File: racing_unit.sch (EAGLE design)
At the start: 45 parts, among them IC1 7805, IC2 7805, IC3 7805, IC4 7805, Q1 MJE2955, Q2 MJE2955, Q3 MJE2955, Q4 MJE2955

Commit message: updated schematic
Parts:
- removed ARD-COIL1, ARD-COIL2, ARD-COIL4, ARD_COIL3: (no value), con-ptr500:AK500/2
- removed C2, C3: 470uF/25V, rcl:CPOL-EUE3.5-8
- added ARDUINI_1-12, ARDUINO_13-24: (no value), pinhead:PINHD-1X12
- added HC-06: (no value), pinhead:PINHD-1X4
- added LED1: (no value), led:LED3MM
- added MPU6050: (no value), pinhead:PINHD-1X8
- added QS_SENSOR: (no value), con-ptr500:AK500/2
- added R13: 150R, resistor:R-EU_0204/5
- added R14: 330R, resistor:R-EU_0204/5
- R6: value 1k -> 2k2
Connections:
- new net N$13: LED1.A, R13.1
- new net N$27: ARDUINI_1-12.6, MPU6050.3, R8.1
- new net N$28: ARDUINI_1-12.2, R5.2
- new net N$30: ARDUINO_13-24.1, C1.+, C4.+, D1.C, D2.C, D3.C, D4.C, R13.2, SUPPLY-1.KL
- new net N$32: HC-06.3, R5.1, R6.1
- net N$16: now also ARDUINO_13-24.8, QS_SENSOR-1.KL, R14.1; no longer ARD-COIL2-1.KL, R6.1
- net N$18: now also ARDUINI_1-12.5, MPU6050.4, R7.1; no longer C1.+, C2.+, C3.+, C4.+, D1.C, D2.C, D3.C, D4.C, SUPPLY-1.KL
- net N$19: now also ARDUINI_1-12.9; no longer R7.2
- net N$20: now also ARDUINI_1-12.10, MPU6050.8; no longer ARD_COIL3-1.KL, R7.1
- net N$22: now also ARDUINI_1-12.1, HC-06.4; no longer ARD-COIL4-1.KL, R8.1
- net N$23: now also ARDUINO_13-24.12; no longer ARD-COIL1-2.KL
- net N$24: now also ARDUINO_13-24.11; no longer ARD-COIL2-2.KL
- net N$25: now also ARDUINO_13-24.10; no longer ARD_COIL3-2.KL
- net N$26: now also ARDUINO_13-24.9; no longer ARD-COIL4-2.KL
- net N$5: now also ARDUINO_13-24.4, HC-06.1, MPU6050.1, MPU6050.7, QS_SENSOR-2.KL, R7.2, R8.2; no longer ARD-COIL1-1.KL, R5.1
- net N$6: now also ARDUINI_1-12.12; no longer R5.2
- net N$7: now also ARDUINI_1-12.11; no longer R6.2
- net N$8: now also ARDUINI_1-12.8; no longer R8.2
- net PE: now also ARDUINI_1-12.3, ARDUINI_1-12.4, ARDUINO_13-24.2, HC-06.2, LED1.C, MPU6050.2, R14.2, R6.2; no longer C2.-, C3.-
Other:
- moved on the sheet: C1, C4, D1, D2, D3, D4, R10, R11, R12, R5, R6, R7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

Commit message: added pcb design
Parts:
- removed C4: 470uF/25V, rcl:CPOL-EUE3.5-8
- removed LED1: (no value), led:LED3MM
- added C2: 4700uF/25V, rcl:CPOL-EUE7.5-16
- added J1, J2: J10MM, jumper:J10MM
- added J3, J4, J7, J8, J9: J5MM, jumper:J5MM
- added J5, J6: J7MM, jumper:J7MM
- added LED: (no value), pinhead:PINHD-1X2
- C1: value 470uF/25V -> 4700uF/25V; device rcl:CPOL-EUE3.5-8 -> rcl:CPOL-EUE7.5-16
- D1, D2, D3, D4: value 1N4007 -> 1N4937
- IC1, IC2, IC3, IC4: value 7805 -> 78L05Z; device v-reg:78XXS -> linear:78L05Z
- Q1, Q2, Q3, Q4: value MJE2955 -> BDX54C
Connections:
- removed net PE: ARDUINI_1-12.3, ARDUINI_1-12.4, ARDUINO_13-24.2, C1.-, C10.2, C11.2, C12.2, C4.-, C5.2, C6.2, C7.2, C8.2, C9.2, HC-06.2, IC1.GND, IC2.GND, IC3.GND, IC4.GND, LED1.C, MPU6050.2, R1.1, R14.2, R2.1, R3.1, R4.1, R6.2, SUPPLY-2.KL
- new net GND: ARDUINI_1-12.3, ARDUINI_1-12.4, ARDUINO_13-24.2, C1.-, C10.2, C11.2, C12.2, C2.-, C5.2, C6.2, C7.2, C8.2, C9.2, HC-06.2, IC1.GND, IC2.GND, IC3.GND, IC4.GND, LED.1, MPU6050.2, R1.1, R14.2, R2.1, R3.1, R4.1, R6.2, SUPPLY-2.KL
- new net N$29: ARDUINI_1-12.12, J3.1, R1.2
- new net N$31: ARDUINI_1-12.11, J4.2, R2.2
- new net N$33: ARDUINI_1-12.9, J5.2, R3.2
- new net N$34: ARDUINI_1-12.8, J6.2, R4.2
- new net N$35: J4.1, J7.1
- new net N$37: J8.2, Q3.B
- new net N$38: J5.1, J8.1
- new net N$40: J9.2, Q4.B
- new net N$41: J6.1, J9.1
- net N$1: now also IC1.VI; no longer IC1.IN
- net N$13: now also LED.2, R13.2; no longer LED1.A, R13.1
- net N$14: now also IC1.VO; no longer IC1.OUT
- net N$15: now also IC2.VO; no longer IC2.OUT
- net N$17: now also IC4.VO; no longer IC4.OUT
- net N$19: now also ARDUINO_13-24.1, C1.+, C2.+, D3.C, D4.C, J2.2, SUPPLY-1.KL; no longer ARDUINI_1-12.9, Q3.B, R3.2
- net N$2: now also IC2.VI; no longer IC2.IN
- net N$21: now also IC3.VO; no longer IC3.OUT
- net N$22: now also R5.2; no longer HC-06.4
- net N$28: now also J3.2, Q1.B; no longer ARDUINI_1-12.2, R5.2
- net N$3: now also IC3.VI; no longer IC3.IN
- net N$30: now also J7.2, Q2.B; no longer ARDUINO_13-24.1, C1.+, C4.+, D1.C, D2.C, D3.C, D4.C, R13.2, SUPPLY-1.KL
- net N$32: now also HC-06.4; no longer HC-06.3
- net N$4: now also IC4.VI; no longer IC4.IN
- net N$6: now also ARDUINI_1-12.2, HC-06.3; no longer ARDUINI_1-12.12, Q1.B, R1.2
- net N$7: now also D1.C, J1.1, R13.1; no longer ARDUINI_1-12.11, Q2.B, R2.2
- net N$8: now also D2.C, J1.2, J2.1; no longer ARDUINI_1-12.8, Q4.B, R4.2
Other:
- moved on the sheet: D4, Q2, Q3, Q4, R10, R11, R12, R13, R5, R6, R9, SUPPLY-1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

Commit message: fixed pcb
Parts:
- removed J6: J7MM, jumper:J7MM
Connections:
- removed net N$31 (its old number): ARDUINI_1-12.11, J4.2, R2.2
- removed net N$34: ARDUINI_1-12.8, J6.2, R4.2
- new net N$18: ARDUINO_13-24.4, J5.2, QS_SENSOR-2.KL, R8.2
- net N$20: now also J3.1; no longer MPU6050.8
- net N$27: now also J4.1; no longer MPU6050.3
- net N$28: now also ARDUINI_1-12.12, R1.2; no longer J3.2
- net N$29: now also J3.2, MPU6050.8; no longer ARDUINI_1-12.12, J3.1, R1.2
- net N$33: now also J4.2, MPU6050.3; no longer ARDUINI_1-12.9, J5.2, R3.2
- net N$35: now also ARDUINI_1-12.11, R2.2; no longer J4.1
- net N$38: now also ARDUINI_1-12.9, R3.2; no longer J5.1
- net N$41: now also ARDUINI_1-12.8, R4.2; no longer J6.1
- net N$5: now also J5.1; no longer ARDUINO_13-24.4, QS_SENSOR-2.KL, R8.2
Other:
- moved on the sheet: J3, J4, J5, R7, R8

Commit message: updated pcb and schematic
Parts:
- J3: value J5MM -> J10MM; device jumper:J5MM -> jumper:J10MM
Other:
- moved on the sheet: C1, C2, SUPPLY-2
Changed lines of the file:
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@@
 <?xml version="1.0" encoding="utf-8"?>
 <!DOCTYPE eagle SYSTEM "eagle.dtd">
-<eagle version="7.6.0">
+<eagle version="7.2.0">
 <drawing>
 <settings>
@@
 <layers>
 <layer number="1" name="Top" color="4" fill="11" visible="no" active="no"/>
+<layer number="2" name="Route2" color="1" fill="3" visible="no" active="no"/>
+<layer number="3" name="Route3" color="4" fill="3" visible="no" active="no"/>
+<layer number="4" name="Route4" color="1" fill="4" visible="no" active="no"/>
+<layer number="5" name="Route5" color="4" fill="4" visible="no" active="no"/>
+<layer number="6" name="Route6" color="1" fill="8" visible="no" active="no"/>
+<layer number="7" name="Route7" color="4" fill="8" visible="no" active="no"/>
+<layer number="8" name="Route8" color="1" fill="2" visible="no" active="no"/>
+<layer number="9" name="Route9" color="4" fill="2" visible="no" active="no"/>
+<layer number="10" name="Route10" color="1" fill="7" visible="no" active="no"/>
+<layer number="11" name="Route11" color="4" fill="7" visible="no" active="no"/>
+<layer number="12" name="Route12" color="1" fill="5" visible="no" active="no"/>
+<layer number="13" name="Route13" color="4" fill="5" visible="no" active="no"/>
+<layer number="14" name="Route14" color="1" fill="6" visible="no" active="no"/>
+<layer number="15" name="Route15" color="4" fill="6" visible="no" active="no"/>
 <layer number="16" name="Bottom" color="1" fill="1" visible="no" active="no"/>
 <layer number="17" name="Pads" color="2" fill="1" visible="no" active="no"/>
@@
 <part name="D3" library="diode" deviceset="1N4004" device="" value="1N4937"/>
 <part name="D4" library="diode" deviceset="1N4004" device="" value="1N4937"/>
-<part name="GND11" library="supply2" deviceset="PE" device="" value="GND"/>
 <part name="SUPPLY" library="con-ptr500" deviceset="AK500/2" device=""/>
 <part name="GND12" library="supply2" deviceset="PE" device="" value="GND"/>
@@
 <part name="GND15" library="supply2" deviceset="PE" device="" value="GND"/>
 <part name="C1" library="rcl" deviceset="CPOL-EU" device="E7.5-16" value="4700uF/25V"/>
-<part name="C2" library="rcl" deviceset="CPOL-EU" device="E7.5-16" value="4700uF/25V"/>
 <part name="IC1" library="linear" deviceset="78*" device="Z" technology="L05"/>
 <part name="IC2" library="linear" deviceset="78*" device="Z" technology="L05"/>
@@
 <part name="J8" library="jumper" deviceset="J" device="5MM"/>
 <part name="J9" library="jumper" deviceset="J" device="5MM"/>
-<part name="J3" library="jumper" deviceset="J" device="5MM"/>
 <part name="J4" library="jumper" deviceset="J" device="5MM"/>
 <part name="J5" library="jumper" deviceset="J" device="7MM"/>
+<part name="J3" library="jumper" deviceset="J" device="10MM"/>
+<part name="C2" library="rcl" deviceset="CPOL-EU" device="E7.5-16" value="4700uF/25V"/>
 </parts>
 <sheets>
@@
 <instance part="D3" gate="1" x="129.54" y="22.86" rot="R270"/>
 <instance part="D4" gate="1" x="180.34" y="22.86" rot="R270"/>
-<instance part="GND11" gate="PE" x="180.34" y="-15.24"/>
 <instance part="SUPPLY" gate="-1" x="195.58" y="-25.4" rot="R90"/>
-<instance part="SUPPLY" gate="-2" x="203.2" y="-25.4" rot="R90"/>
-<instance part="GND12" gate="PE" x="213.36" y="-2.54"/>
+<instance part="SUPPLY" gate="-2" x="200.66" y="-25.4" rot="R90"/>
+<instance part="GND12" gate="PE" x="205.74" y="-2.54"/>
 <instance part="COIL1" gate="-1" x="15.24" y="111.76" rot="R270"/>
 <instance part="COIL1" gate="-2" x="20.32" y="111.76" rot="R270"/>
@@
 <instance part="GND9" gate="PE" x="22.86" y="-35.56"/>
 <instance part="R14" gate="G$1" x="137.16" y="-30.48" rot="R90"/>
-<instance part="GND10" gate="PE" x="162.56" y="-15.24"/>
+<instance part="GND10" gate="PE" x="180.34" y="-20.32"/>
 <instance part="GND13" gate="PE" x="40.64" y="-33.02"/>
 <instance part="GND14" gate="PE" x="152.4" y="-30.48"/>
 <instance part="GND15" gate="PE" x="137.16" y="-50.8"/>
-<instance part="C1" gate="G$1" x="162.56" y="-2.54"/>
-<instance part="C2" gate="G$1" x="180.34" y="-2.54"/>
+<instance part="C1" gate="G$1" x="180.34" y="-2.54"/>
 <instance part="IC1" gate="A1" x="38.1" y="99.06"/>
 <instance part="IC2" gate="A1" x="86.36" y="99.06"/>
@@
 <instance part="J8" gate="1" x="91.44" y="60.96"/>
 <instance part="J9" gate="1" x="139.7" y="60.96"/>
-<instance part="J3" gate="1" x="73.66" y="-68.58"/>
 <instance part="J4" gate="1" x="129.54" y="-55.88"/>
 <instance part="J5" gate="1" x="121.92" y="-25.4" rot="R90"/>
+<instance part="J3" gate="1" x="73.66" y="-68.58"/>
+<instance part="C2" gate="G$1" x="162.56" y="-2.54"/>
 </instances>
 <busses>
@@
 </segment>
 <segment>
-<pinref part="GND11" gate="PE" pin="PE"/>
-<wire x1="180.34" y1="-7.62" x2="180.34" y2="-12.7" width="0.1524" layer="91"/>
-<pinref part="C2" gate="G$1" pin="-"/>
-</segment>
-<segment>
 <pinref part="GND12" gate="PE" pin="PE"/>
-<wire x1="213.36" y1="0" x2="213.36" y2="5.08" width="0.1524" layer="91"/>
+<wire x1="205.74" y1="0" x2="205.74" y2="5.08" width="0.1524" layer="91"/>
 <pinref part="SUPPLY" gate="-2" pin="KL"/>
-<wire x1="213.36" y1="5.08" x2="203.2" y2="5.08" width="0.1524" layer="91"/>
-<wire x1="203.2" y1="5.08" x2="203.2" y2="-20.32" width="0.1524" layer="91"/>
+<wire x1="205.74" y1="5.08" x2="200.66" y2="5.08" width="0.1524" layer="91"/>
+<wire x1="200.66" y1="5.08" x2="200.66" y2="-20.32" width="0.1524" layer="91"/>
 </segment>
 <segment>
@@
 <segment>
 <pinref part="GND10" gate="PE" pin="PE"/>
+<wire x1="180.34" y1="-7.62" x2="180.34" y2="-12.7" width="0.1524" layer="91"/>
+<pinref part="C1" gate="G$1" pin="-"/>
+<pinref part="C2" gate="G$1" pin="-"/>
+<wire x1="180.34" y1="-12.7" x2="180.34" y2="-17.78" width="0.1524" layer="91"/>
 <wire x1="162.56" y1="-7.62" x2="162.56" y2="-12.7" width="0.1524" layer="91"/>
-<pinref part="C1" gate="G$1" pin="-"/>
+<wire x1="162.56" y1="-12.7" x2="180.34" y2="-12.7" width="0.1524" layer="91"/>
+<junction x="180.34" y="-12.7"/>
 </segment>
 <segment>
@@
 <pinref part="ARDUINI_1-12" gate="G$1" pin="10"/>
 <wire x1="48.26" y1="-43.18" x2="55.88" y2="-43.18" width="0.1524" layer="91"/>
+<wire x1="48.26" y1="-68.58" x2="68.58" y2="-68.58" width="0.1524" layer="91"/>
 <pinref part="J3" gate="1" pin="1"/>
-<wire x1="48.26" y1="-68.58" x2="68.58" y2="-68.58" width="0.1524" layer="91"/>
 </segment>
 </net>
@@
 <pinref part="D4" gate="1" pin="C"/>
 <wire x1="129.54" y1="5.08" x2="162.56" y2="5.08" width="0.1524" layer="91"/>
+<pinref part="D3" gate="1" pin="C"/>
 <wire x1="162.56" y1="5.08" x2="180.34" y2="5.08" width="0.1524" layer="91"/>
-<pinref part="D3" gate="1" pin="C"/>
 <wire x1="180.34" y1="5.08" x2="180.34" y2="20.32" width="0.1524" layer="91"/>
 <wire x1="129.54" y1="20.32" x2="129.54" y2="5.08" width="0.1524" layer="91"/>
@@
 <junction x="180.34" y="5.08"/>
 <junction x="180.34" y="5.08"/>
-<wire x1="162.56" y1="5.08" x2="162.56" y2="0" width="0.1524" layer="91"/>
-<junction x="162.56" y="5.08"/>
+<wire x1="180.34" y1="5.08" x2="180.34" y2="0" width="0.1524" layer="91"/>
+<junction x="180.34" y="5.08"/>
 <pinref part="C1" gate="G$1" pin="+"/>
-<pinref part="C2" gate="G$1" pin="+"/>
-<wire x1="180.34" y1="0" x2="180.34" y2="5.08" width="0.1524" layer="91"/>
 <junction x="180.34" y="5.08"/>
 <pinref part="J2" gate="1" pin="2"/>
@@
 <wire x1="96.52" y1="-15.24" x2="129.54" y2="-15.24" width="0.1524" layer="91"/>
 <wire x1="129.54" y1="-15.24" x2="129.54" y2="5.08" width="0.1524" layer="91"/>
+<wire x1="162.56" y1="0" x2="162.56" y2="5.08" width="0.1524" layer="91"/>
+<junction x="162.56" y="5.08"/>
+<pinref part="C2" gate="G$1" pin="+"/>
 </segment>
 </net>
@@
 <net name="N$29" class="0">
 <segment>
-<pinref part="J3" gate="1" pin="2"/>
 <pinref part="MPU6050" gate="A" pin="8"/>
 <wire x1="78.74" y1="-68.58" x2="152.4" y2="-68.58" width="0.1524" layer="91"/>
-</segment>
-</net>
+<pinref part="J3" gate="1" pin="2"/>
+</segment>
+</net>

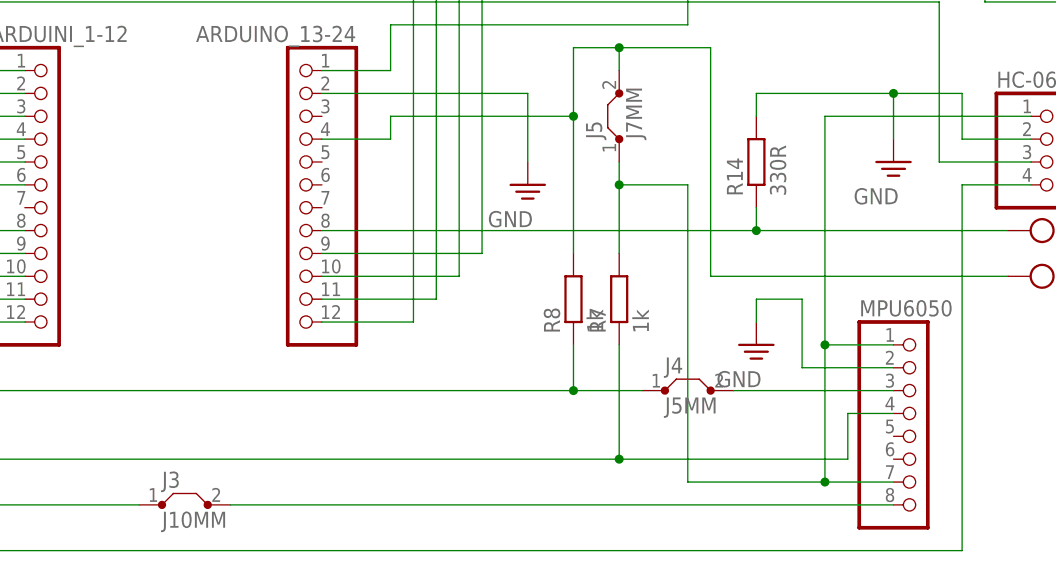
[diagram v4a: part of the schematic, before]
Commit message: updated pcb and improved spark killing procedure
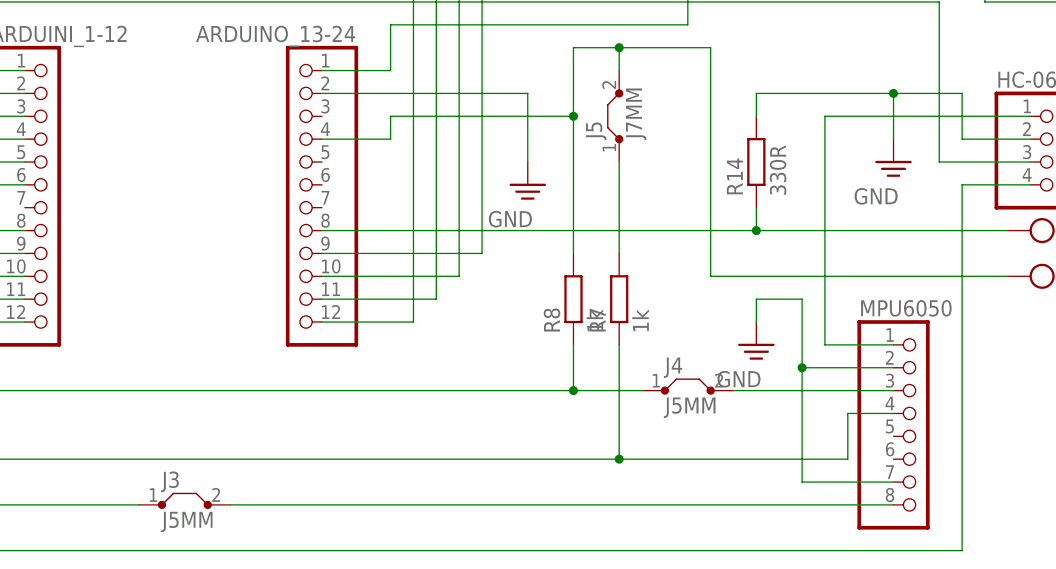
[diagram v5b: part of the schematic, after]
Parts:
- J3: value J10MM -> J5MM; device jumper:J10MM -> jumper:J5MM
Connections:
- removed net N$5: HC-06.1, J5.1, MPU6050.1, MPU6050.7, R7.2
- new net N$34: HC-06.1, MPU6050.1
- new net N$36: J5.1, R7.2
- net GND: now also MPU6050.7
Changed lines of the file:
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@@
 <part name="J4" library="jumper" deviceset="J" device="5MM"/>
 <part name="J5" library="jumper" deviceset="J" device="7MM"/>
-<part name="J3" library="jumper" deviceset="J" device="10MM"/>
 <part name="C2" library="rcl" deviceset="CPOL-EU" device="E7.5-16" value="4700uF/25V"/>
+<part name="J3" library="jumper" deviceset="J" device="5MM"/>
 </parts>
 <sheets>
@@
 <instance part="J4" gate="1" x="129.54" y="-55.88"/>
 <instance part="J5" gate="1" x="121.92" y="-25.4" rot="R90"/>
+<instance part="C2" gate="G$1" x="162.56" y="-2.54"/>
 <instance part="J3" gate="1" x="73.66" y="-68.58"/>
-<instance part="C2" gate="G$1" x="162.56" y="-2.54"/>
 </instances>
 <busses>
@@
 <wire x1="142.24" y1="-45.72" x2="142.24" y2="-53.34" width="0.1524" layer="91"/>
 <wire x1="142.24" y1="-53.34" x2="152.4" y2="-53.34" width="0.1524" layer="91"/>
+<pinref part="MPU6050" gate="A" pin="7"/>
+<wire x1="142.24" y1="-66.04" x2="152.4" y2="-66.04" width="0.1524" layer="91"/>
+<wire x1="142.24" y1="-66.04" x2="142.24" y2="-53.34" width="0.1524" layer="91"/>
+<junction x="142.24" y="-53.34"/>
 </segment>
 <segment>
@@
 </segment>
 </net>
-<net name="N$5" class="0">
-<segment>
-<pinref part="MPU6050" gate="A" pin="7"/>
-<wire x1="152.4" y1="-66.04" x2="144.78" y2="-66.04" width="0.1524" layer="91"/>
+<net name="N$34" class="0">
+<segment>
 <pinref part="HC-06" gate="A" pin="1"/>
 <wire x1="167.64" y1="-25.4" x2="144.78" y2="-25.4" width="0.1524" layer="91"/>
 <wire x1="144.78" y1="-25.4" x2="144.78" y2="-50.8" width="0.1524" layer="91"/>
-<junction x="144.78" y="-50.8"/>
 <pinref part="MPU6050" gate="A" pin="1"/>
 <wire x1="152.4" y1="-50.8" x2="144.78" y2="-50.8" width="0.1524" layer="91"/>
-<wire x1="144.78" y1="-50.8" x2="144.78" y2="-66.04" width="0.1524" layer="91"/>
-<junction x="144.78" y="-66.04"/>
-<wire x1="129.54" y1="-66.04" x2="144.78" y2="-66.04" width="0.1524" layer="91"/>
-<wire x1="129.54" y1="-66.04" x2="129.54" y2="-33.02" width="0.1524" layer="91"/>
+</segment>
+</net>
+<net name="N$36" class="0">
+<segment>
+<pinref part="J5" gate="1" pin="1"/>
 <pinref part="R7" gate="G$1" pin="2"/>
-<pinref part="J5" gate="1" pin="1"/>
-<wire x1="121.92" y1="-40.64" x2="121.92" y2="-33.02" width="0.1524" layer="91"/>
-<wire x1="121.92" y1="-33.02" x2="121.92" y2="-30.48" width="0.1524" layer="91"/>
-<wire x1="129.54" y1="-33.02" x2="121.92" y2="-33.02" width="0.1524" layer="91"/>
-<junction x="121.92" y="-33.02"/>
-</segment>
-</net>
+<wire x1="121.92" y1="-40.64" x2="121.92" y2="-30.48" width="0.1524" layer="91"/>
+</segment>
+</net>
